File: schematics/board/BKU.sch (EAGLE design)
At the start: 71 parts

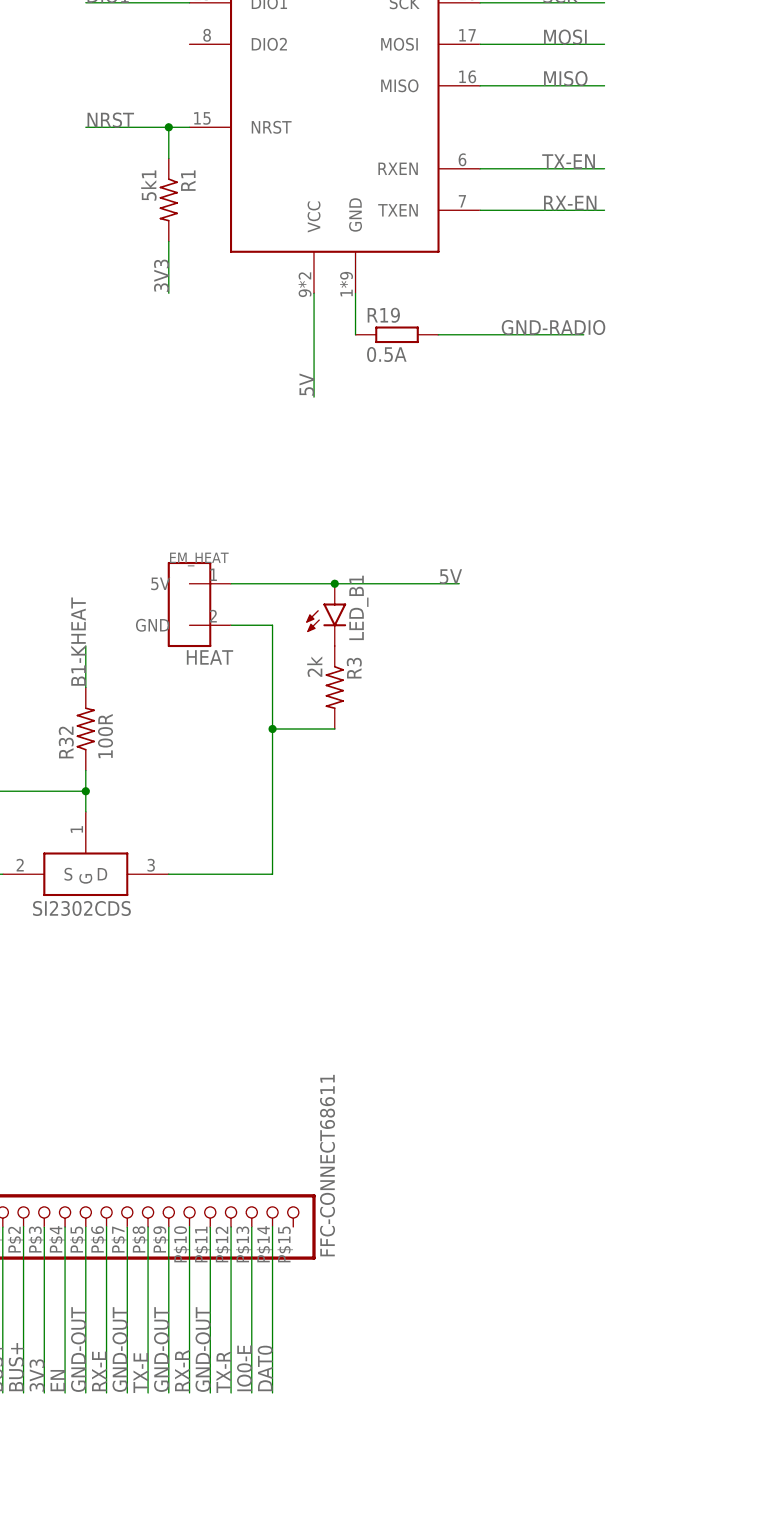
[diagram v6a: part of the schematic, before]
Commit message: Обновлена схема БКУ
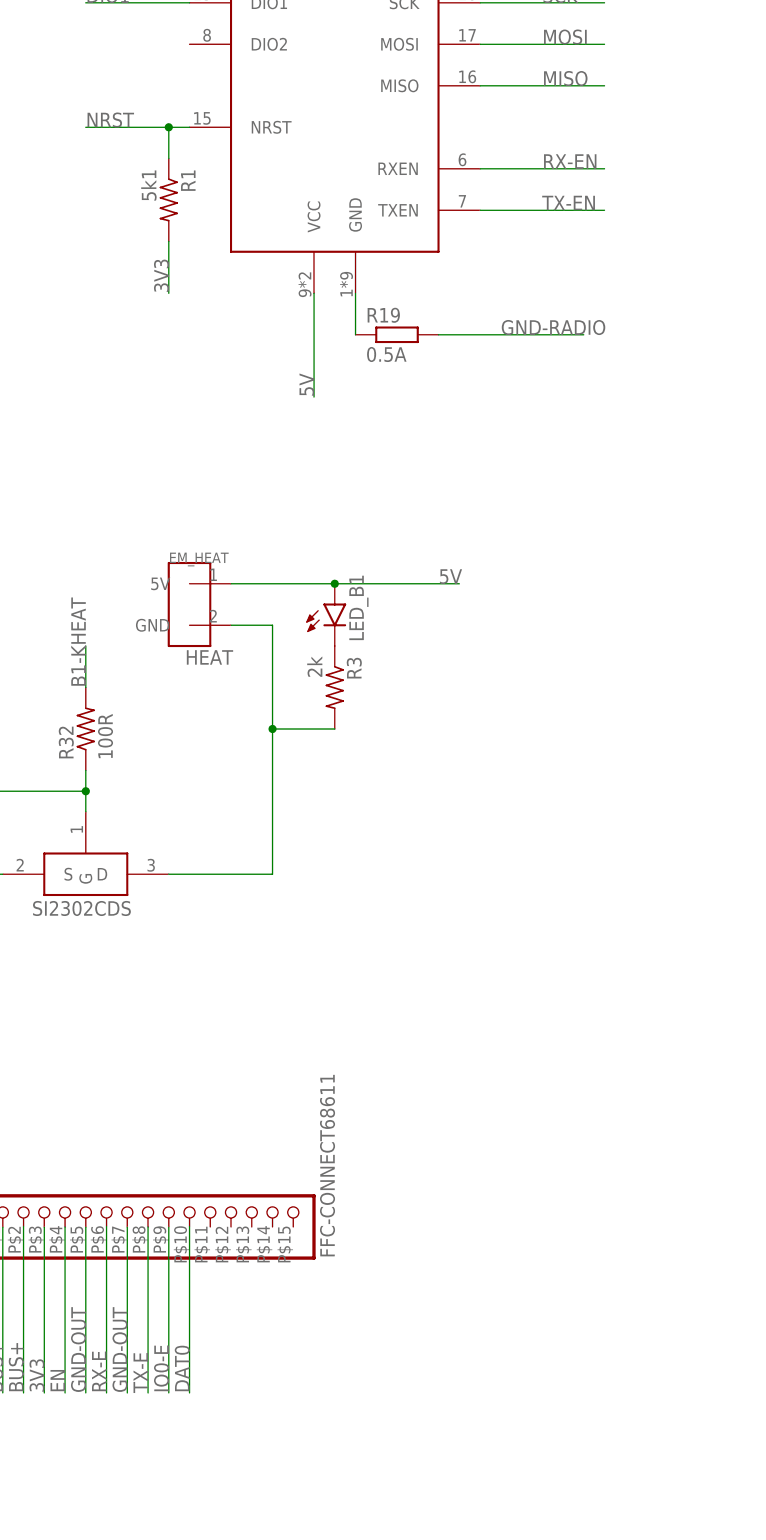
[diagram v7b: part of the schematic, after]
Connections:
- removed net RX-R: U$21.10
- removed net TX-R: U$21.12
- net DAT0: now also U$21.10; no longer U$21.14
- net GND-OUT: no longer U$21.11, U$21.9
- net IO0-E: now also U$21.9; no longer U$21.13
- net RX-EN: now also U$1.RXEN; no longer U$1.TXEN
- net TX-EN: now also U$1.TXEN; no longer U$1.RXEN
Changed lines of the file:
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@@
 </segment>
 <segment>
-<wire x1="360.68" y1="106.68" x2="360.68" y2="86.36" width="0.1524" layer="91"/>
-<pinref part="U$21" gate="G$1" pin="14"/>
-<label x="360.68" y="86.36" size="1.778" layer="95" rot="R90"/>
+<wire x1="350.52" y1="106.68" x2="350.52" y2="86.36" width="0.1524" layer="91"/>
+<label x="350.52" y="86.36" size="1.778" layer="95" rot="R90"/>
+<pinref part="U$21" gate="G$1" pin="10"/>
 </segment>
 </net>
@@
 </segment>
 <segment>
-<wire x1="358.14" y1="106.68" x2="358.14" y2="86.36" width="0.1524" layer="91"/>
-<pinref part="U$21" gate="G$1" pin="13"/>
-<label x="358.14" y="86.36" size="1.778" layer="95" rot="R90"/>
+<wire x1="347.98" y1="106.68" x2="347.98" y2="86.36" width="0.1524" layer="91"/>
+<label x="347.98" y="86.36" size="1.778" layer="95" rot="R90"/>
+<pinref part="U$21" gate="G$1" pin="9"/>
 </segment>
 </net>
@@
 <pinref part="U$20" gate="G$1" pin="DS"/>
 <wire x1="134.62" y1="187.96" x2="132.08" y2="187.96" width="0.1524" layer="91"/>
-</segment>
-</net>
-<net name="TX-R" class="0">
-<segment>
-<wire x1="355.6" y1="106.68" x2="355.6" y2="86.36" width="0.1524" layer="91"/>
-<label x="355.6" y="86.36" size="1.778" layer="95" rot="R90"/>
-<pinref part="U$21" gate="G$1" pin="12"/>
-</segment>
-</net>
-<net name="RX-R" class="0">
-<segment>
-<wire x1="350.52" y1="106.68" x2="350.52" y2="86.36" width="0.1524" layer="91"/>
-<label x="350.52" y="86.36" size="1.778" layer="95" rot="R90"/>
-<pinref part="U$21" gate="G$1" pin="10"/>
 </segment>
 </net>
@@
 </segment>
 <segment>
+<pinref part="U$1" gate="G$1" pin="RXEN"/>
+<wire x1="386.08" y1="236.22" x2="401.32" y2="236.22" width="0.1524" layer="91"/>
+<label x="393.7" y="236.22" size="1.778" layer="95"/>
+</segment>
+</net>
+<net name="TX-EN" class="0">
+<segment>
+<wire x1="144.78" y1="71.12" x2="152.4" y2="71.12" width="0.1524" layer="91"/>
+<label x="147.32" y="71.12" size="1.778" layer="95"/>
+<pinref part="U$13" gate="G$1" pin="IO25"/>
+</segment>
+<segment>
 <pinref part="U$1" gate="G$1" pin="TXEN"/>
 <wire x1="386.08" y1="231.14" x2="401.32" y2="231.14" width="0.1524" layer="91"/>
 <label x="393.7" y="231.14" size="1.778" layer="95"/>
-</segment>
-</net>
-<net name="TX-EN" class="0">
-<segment>
-<wire x1="144.78" y1="71.12" x2="152.4" y2="71.12" width="0.1524" layer="91"/>
-<label x="147.32" y="71.12" size="1.778" layer="95"/>
-<pinref part="U$13" gate="G$1" pin="IO25"/>
-</segment>
-<segment>
-<pinref part="U$1" gate="G$1" pin="RXEN"/>
-<wire x1="386.08" y1="236.22" x2="401.32" y2="236.22" width="0.1524" layer="91"/>
-<label x="393.7" y="236.22" size="1.778" layer="95"/>
 </segment>
 </net>
@@
 </segment>
 <segment>
-<wire x1="347.98" y1="106.68" x2="347.98" y2="86.36" width="0.1524" layer="91"/>
-<label x="347.98" y="86.36" size="1.778" layer="95" rot="R90"/>
-<pinref part="U$21" gate="G$1" pin="9"/>
-</segment>
-<segment>
-<wire x1="353.06" y1="106.68" x2="353.06" y2="86.36" width="0.1524" layer="91"/>
-<label x="353.06" y="86.36" size="1.778" layer="95" rot="R90"/>
-<pinref part="U$21" gate="G$1" pin="11"/>
-</segment>
-<segment>

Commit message: Завершена разработка плат БСК5 и АРК, половина платы БКУ разведена, добавлены гербер файлы плат АРК, БСК5 и WSPR
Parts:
- added MP1584EN-5V: MP1584-B, CanCubeSat:MP1584-B
- renumbered MP2225 to MP2225-3V3, MP2225-1 to MP2225-5V, U$6 to MP1584EN-3V3
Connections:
- removed net N$21: C10.2, C9.2, MP2225-3V3.IN, R16.1
- removed net N$7: C14.2, C6.2, MP2225-5V.IN, R27.1
- new net GND1-RADIO: R19.1, U$1.GND
- net 5V: now also MP1584EN-5V.OUT+, U$21.11
- net BUS+: now also C10.2, C14.2, C6.2, C9.2, MP1584EN-5V.IN+, MP2225-3V3.IN, MP2225-5V.IN, R16.1, R27.1
- net GND: no longer C12.1, R19.1, U$1.GND
- net GND-OUT: now also MP1584EN-5V.IN-, MP1584EN-5V.OUT-
- net N$5: now also C12.1
